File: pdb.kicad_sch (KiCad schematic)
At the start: 0 parts

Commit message: first commit branch
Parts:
- added F1: Fuse, Library:FUSE-TH_XF-508P-A-B, symbol Device:Fuse
- added J1: Amass Elec AS150UPW(2+4), Library:CONN-TH_AS150UPW, symbol Connector:Conn_01x06_Pin
- added J2, J3, J4, J5: BOOMELE 4.2-2*3AW, Connector_Molex:Molex_Mini-Fit_Jr_5569-06A2_2x03_P4.20mm_Horizontal, symbol Connector:Conn_01x06_Pin
- added J6: Conn_01x08_Pin, symbol Connector:Conn_01x08_Pin
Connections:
- new net +BATT: F1.1, J1.2 (Pin_2)
- new net CAN_H_1: J1.3 (Pin_3), J2.1 (Pin_1)
- new net CAN_H_2: J2.3 (Pin_3), J3.1 (Pin_1)
- new net CAN_H_3: J3.3 (Pin_3), J4.1 (Pin_1)
- new net CAN_H_4: J4.3 (Pin_3), J5.1 (Pin_1)
- new net CAN_H_5: J5.3 (Pin_3), J6.3 (Pin_3)
- new net CAN_H_6: J6.5 (Pin_5)
- new net CAN_L_1: J1.4 (Pin_4), J2.2 (Pin_2)
- new net CAN_L_2: J2.4 (Pin_4), J3.2 (Pin_2)
- new net CAN_L_3: J3.4 (Pin_4), J4.2 (Pin_2)
- new net CAN_L_4: J4.4 (Pin_4), J5.2 (Pin_2)
- new net CAN_L_5: J5.4 (Pin_4), J6.4 (Pin_4)
- new net CAN_L_6: J6.6 (Pin_6)
- new net GND: J1.1 (Pin_1), J2.6 (Pin_6), J3.6 (Pin_6), J4.6 (Pin_6), J5.6 (Pin_6), J6.1 (Pin_1), J6.7 (Pin_7)
- new net PWM_Mot_BL: J5.5 (Pin_5)
- new net PWM_Mot_BR: J4.5 (Pin_5)
- new net PWM_Mot_FL: J3.5 (Pin_5)
- new net PWM_Mot_FR: J2.5 (Pin_5)
- new net PWM_Pump: J6.2 (Pin_2)
- new net VBat: F1.2
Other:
- note added: "Comienza el CAN BUS"
- note added: "MotorBL"
- note added: "MotorBR"
- note added: "MotorFL"
- note added: "MotorFR"
- note added: "Pump"

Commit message: ADD: Mas conectores al esquematico y fuse holder para 10x38
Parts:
- added J10, J16, J7, J8, J9: BOOMELE 4.2-2*4AW, symbol Connector:Conn_01x08_Pin
- added J11: MOLEX 39301240, symbol Connector:Conn_01x24_Pin
- added J12, J13: BOOMELE 4.2-2*2AW, symbol Connector:Conn_01x04_Pin
- added J14, J15: BOOMELE 4.2-2*3AW, Connector_Molex:Molex_Mini-Fit_Jr_5569-06A2_2x03_P4.20mm_Horizontal, symbol Connector:Conn_01x06_Pin
- F1: footprint Library:FUSE-TH_XF-508P-A-B -> Library:FUSE-HOLDER XFCN XF-008; LCSC Part # C19727304 -> C717029
- J6: value Conn_01x08_Pin -> BOOMELE 4.2-2*4AW; LCSC Part # (none) -> C44253
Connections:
- net CAN_H_6: now also J7.3 (Pin_3)
- net CAN_L_6: now also J7.4 (Pin_4)
- net GND: now also J10.1 (Pin_1), J10.7 (Pin_7), J12.2 (Pin_2), J12.4 (Pin_4), J13.2 (Pin_2), J13.4 (Pin_4), J14.2 (Pin_2), J14.5 (Pin_5), J15.2 (Pin_2), J15.5 (Pin_5), J16.1 (Pin_1), J16.8 (Pin_8), J7.1 (Pin_1), J7.7 (Pin_7), J8.1 (Pin_1), J8.7 (Pin_7), J9.1 (Pin_1), J9.7 (Pin_7)
- net VBat: now also J6.8 (Pin_8), J10.8 (Pin_8), J12.1 (Pin_1), J13.1 (Pin_1), J7.8 (Pin_8), J8.8 (Pin_8), J9.8 (Pin_8)
- new net +24V: J16.2 (Pin_2)
- new net +5V: J14.1 (Pin_1), J15.1 (Pin_1)
- new net CAMERA_RX: J16.3 (Pin_3)
- new net CAMERA_Sbus_in: J16.6 (Pin_6)
- new net CAMERA_Sbus_out: J16.5 (Pin_5)
- new net CAMERA_TX: J16.4 (Pin_4)
- new net CAN_H_10: J10.5 (Pin_5)
- new net CAN_H_7: J7.5 (Pin_5), J8.3 (Pin_3)
- new net CAN_H_8: J8.5 (Pin_5), J9.3 (Pin_3)
- new net CAN_H_9: J10.3 (Pin_3), J9.5 (Pin_5)
- new net CAN_L_10: J10.6 (Pin_6)
- new net CAN_L_7: J7.6 (Pin_6), J8.4 (Pin_4)
- new net CAN_L_8: J8.6 (Pin_6), J9.4 (Pin_4)
- new net CAN_L_9: J10.4 (Pin_4), J9.6 (Pin_6)
- new net LIDAR_1_RX_SCL: J14.3 (Pin_3)
- new net LIDAR_1_TX_SDA: J14.4 (Pin_4)
- new net LIDAR_2_RX_SCL: J15.3 (Pin_3)
- new net LIDAR_2_TX_SDA: J15.4 (Pin_4)
- new net PWM_Asp_BL: J10.2 (Pin_2)
- new net PWM_Asp_BR: J9.2 (Pin_2)
- new net PWM_Asp_FL: J8.2 (Pin_2)
- new net PWM_Asp_FR: J7.2 (Pin_2)
- new net PWM_Light: J12.3 (Pin_3), J13.3 (Pin_3)
- no-connect marks 0 -> 2
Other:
- note added: "AspBL"
- note added: "AspBR"
- note added: "AspFL"
- note added: "AspFR"
- note added: "BOM x2"
- note added: "Camera"
- note added: "Lidar 1"
- note added: "Lidar 2"
- note added: "Light 1"
- note added: "Light 2"
- note added: "Veronte"
- moved on the sheet: J6

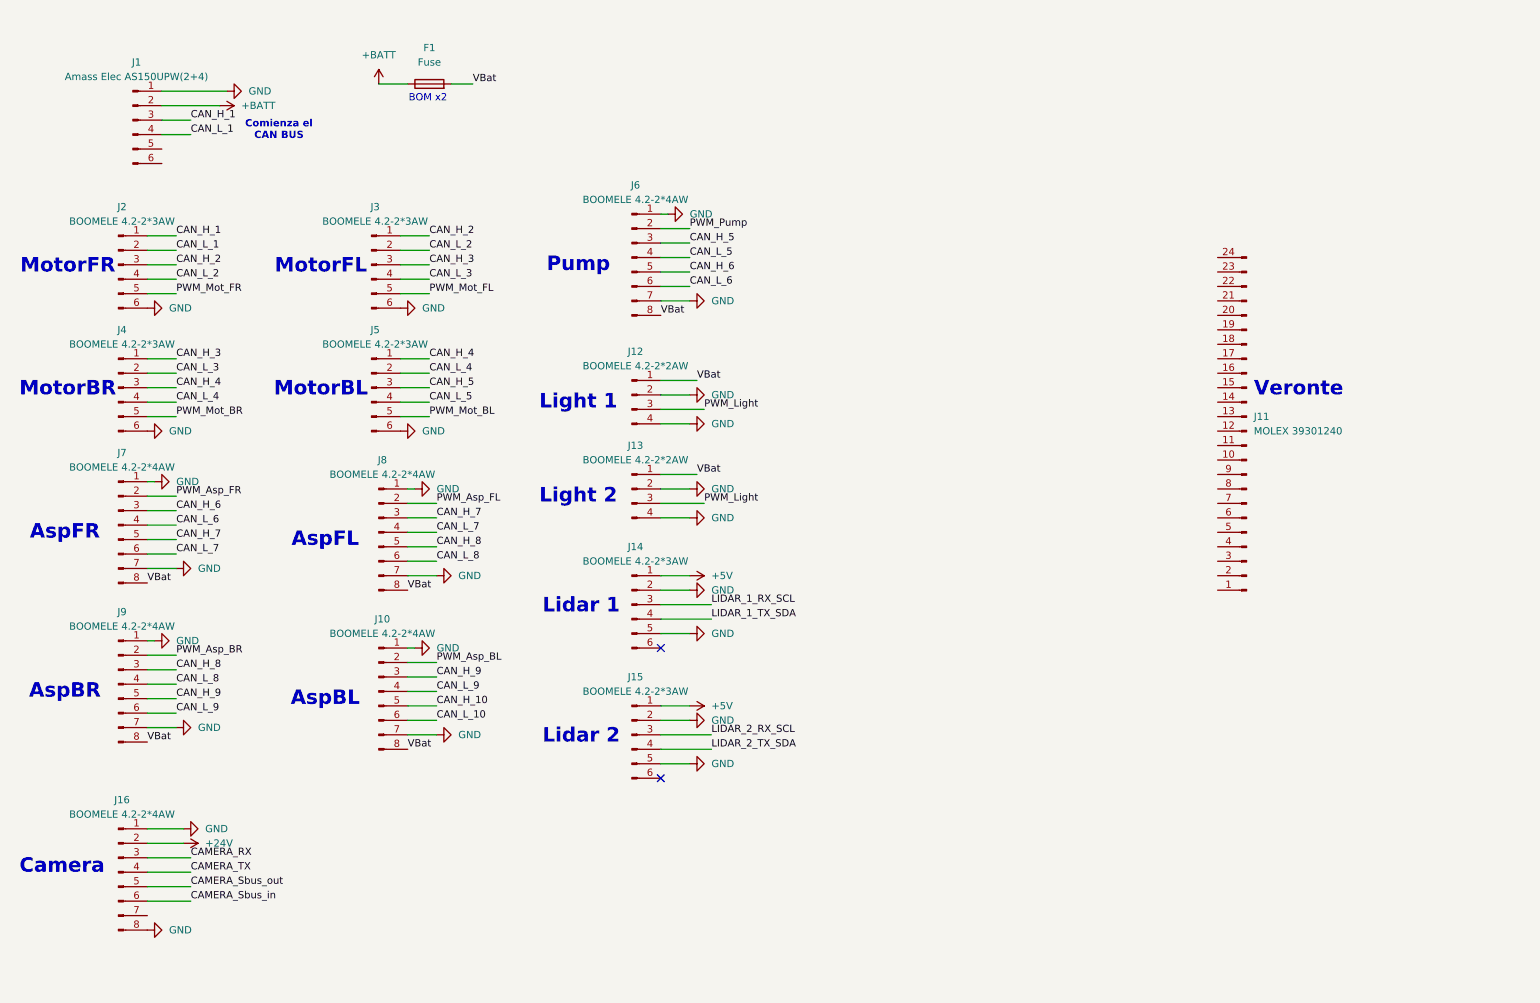
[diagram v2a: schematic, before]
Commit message: Esquematico casi terminado falta agregar el veronte
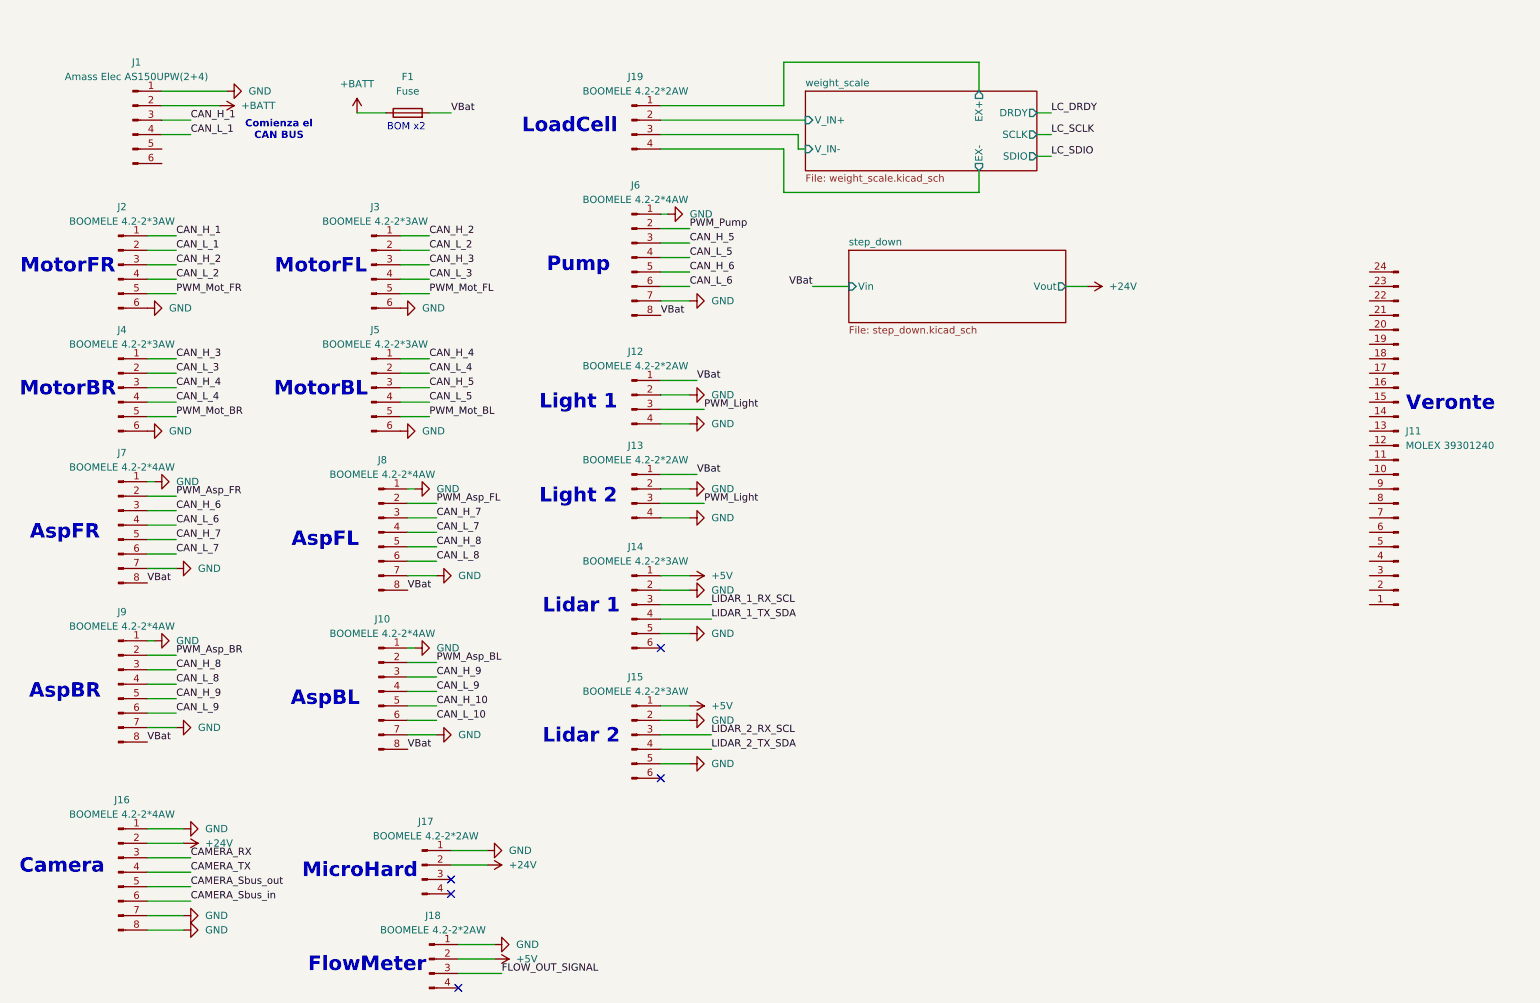
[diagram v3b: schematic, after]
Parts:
- added J17, J18, J19: BOOMELE 4.2-2*2AW, Connector_Molex:Molex_Mini-Fit_Jr_5569-04A2_2x02_P4.20mm_Horizontal, symbol Connector:Conn_01x04_Pin
- J10, J16, J6, J7, J8, J9: footprint (none) -> Connector_Molex:Molex_Mini-Fit_Jr_5569-08A2_2x04_P4.20mm_Horizontal
- J11: footprint (none) -> Connector_Molex:Molex_Mini-Fit_Jr_5569-24A2_2x12_P4.20mm_Horizontal
- J12, J13: footprint (none) -> Connector_Molex:Molex_Mini-Fit_Jr_5569-04A2_2x02_P4.20mm_Horizontal
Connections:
- net +24V: now also J17.2 (Pin_2)
- net +5V: now also J18.2 (Pin_2)
- net GND: now also J16.7 (Pin_7), J17.1 (Pin_1), J18.1 (Pin_1)
- new net FLOW_OUT_SIGNAL: J18.3 (Pin_3)
- new net weight_scale/EX+: J19.1 (Pin_1)
- new net weight_scale/EX-: J19.4 (Pin_4)
- new net weight_scale/V_IN+: J19.2 (Pin_2)
- new net weight_scale/V_IN-: J19.3 (Pin_3)
- no-connect marks 2 -> 5
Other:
- added sheet step_down (step_down.kicad_sch)
- added sheet weight_scale (weight_scale.kicad_sch)
- note added: "FlowMeter"
- note added: "LoadCell"
- note added: "MicroHard"
- moved on the sheet: F1, J11

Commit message: ADD: Fuente de 24V a 5V para los Lidar
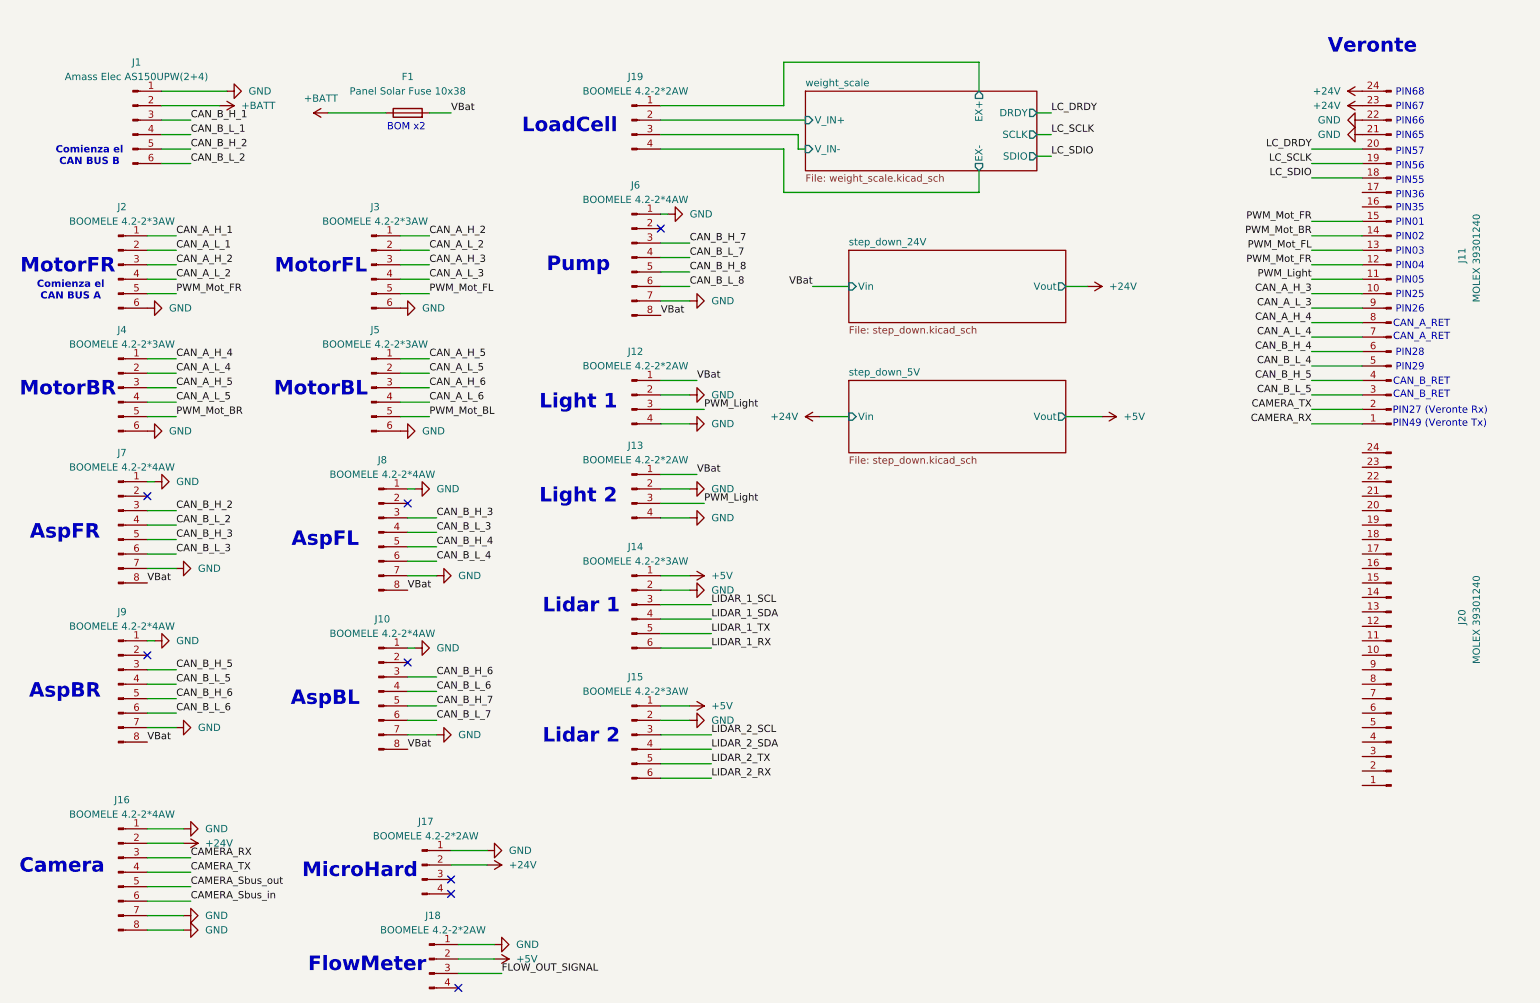
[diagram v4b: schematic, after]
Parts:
- added J20: MOLEX 39301240, Connector_Molex:Molex_Mini-Fit_Jr_5569-24A2_2x12_P4.20mm_Horizontal, symbol Connector:Conn_01x24_Pin
- F1: value Fuse -> Panel Solar Fuse 10x38
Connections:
- net +24V: now also J11.23 (Pin_23), J11.24 (Pin_24)
- net CAMERA_RX: now also J11.1 (Pin_1)
- net CAMERA_TX: now also J11.2 (Pin_2)
- net GND: now also J11.21 (Pin_21), J11.22 (Pin_22); no longer J14.5 (Pin_5), J15.5 (Pin_5)
- net LC_DRDY: now also J11.20 (Pin_20)
- net LC_SCLK: now also J11.19 (Pin_19)
- net LC_SDIO: now also J11.18 (Pin_18)
- net PWM_Light: now also J11.11 (Pin_11)
- net PWM_Mot_BR: now also J11.14 (Pin_14)
- net PWM_Mot_FL: now also J11.13 (Pin_13)
- net PWM_Mot_FR: now also J11.12 (Pin_12), J11.15 (Pin_15)
- net LIDAR_1_RX: now reaches J14.6 (Pin_6)
- net CAN_A_H_3: now reaches J11.10 (Pin_10)
- net CAN_A_H_3: now also J3.3 (Pin_3)
- net CAN_B_L_5: now reaches J11.3 (Pin_3)
- net CAN_B_L_5: now also J9.4 (Pin_4)
- net CAN_B_H_5: now reaches J11.4 (Pin_4)
- net CAN_B_H_5: now also J9.3 (Pin_3)
- net CAN_B_L_4: now reaches J11.5 (Pin_5)
- net CAN_B_L_4: now also J8.6 (Pin_6)
- net CAN_B_H_4: now reaches J11.6 (Pin_6)
- net CAN_B_H_4: now also J8.5 (Pin_5)
- net CAN_A_L_4: now reaches J11.7 (Pin_7)
- net CAN_A_L_4: now also J4.2 (Pin_2)
- net CAN_A_H_4: now reaches J11.8 (Pin_8)
- net CAN_A_H_4: now also J4.1 (Pin_1)
- net CAN_A_L_3: now reaches J11.9 (Pin_9)
- net CAN_A_L_3: now also J3.4 (Pin_4)
- net CAN_B_H_2: now reaches J1.5 (Pin_5)
- net CAN_B_H_2: now also J7.3 (Pin_3)
- net CAN_B_L_2: now reaches J1.6 (Pin_6)
- net CAN_B_L_2: now also J7.4 (Pin_4)
- net LIDAR_2_RX: now reaches J15.6 (Pin_6)
- net CAN_H_1 renamed CAN_A_H_1
- net CAN_A_H_1: no longer J1.3 (Pin_3)
- net CAN_H_10 renamed CAN_B_H_7
- net CAN_B_H_7: now also J6.3 (Pin_3)
- net CAN_H_2 renamed CAN_A_H_2
- removed net CAN_H_3: J3.3 (Pin_3), J4.1 (Pin_1)
- net CAN_H_4 renamed CAN_A_H_5
- net CAN_H_5 renamed CAN_A_H_6
- net CAN_A_H_6: no longer J6.3 (Pin_3)
- net CAN_H_6 renamed CAN_B_H_8
- net CAN_B_H_8: no longer J7.3 (Pin_3)
- net CAN_H_7 renamed CAN_B_H_3
- removed net CAN_H_8: J8.5 (Pin_5), J9.3 (Pin_3)
- net CAN_H_9 renamed CAN_B_H_6
- net CAN_L_1 renamed CAN_A_L_1
- net CAN_A_L_1: no longer J1.4 (Pin_4)
- net CAN_L_10 renamed CAN_B_L_7
- net CAN_B_L_7: now also J6.4 (Pin_4)
- net CAN_L_2 renamed CAN_A_L_2
- removed net CAN_L_3: J3.4 (Pin_4), J4.2 (Pin_2)
- net CAN_L_4 renamed CAN_A_L_5
- net CAN_L_5 renamed CAN_A_L_6
- net CAN_A_L_6: no longer J6.4 (Pin_4)
- net CAN_L_6 renamed CAN_B_L_8
- net CAN_B_L_8: no longer J7.4 (Pin_4)
- net CAN_L_7 renamed CAN_B_L_3
- removed net CAN_L_8: J8.6 (Pin_6), J9.4 (Pin_4)
- net CAN_L_9 renamed CAN_B_L_6
- net LIDAR_1_RX_SCL renamed LIDAR_1_SCL
- net LIDAR_1_TX_SDA renamed LIDAR_1_SDA
- net LIDAR_2_RX_SCL renamed LIDAR_2_SCL
- net LIDAR_2_TX_SDA renamed LIDAR_2_SDA
- net PWM_Asp_BL: no longer names the net of J10.2 (Pin_2)
- net PWM_Asp_BR: no longer names the net of J9.2 (Pin_2)
- net PWM_Asp_FL: no longer names the net of J8.2 (Pin_2)
- net PWM_Asp_FR: no longer names the net of J7.2 (Pin_2)
- net PWM_Pump: no longer names the net of J6.2 (Pin_2)
- new net CAN_B_H_1: J1.3 (Pin_3)
- new net CAN_B_L_1: J1.4 (Pin_4)
- new net LIDAR_1_TX: J14.5 (Pin_5)
- new net LIDAR_2_TX: J15.5 (Pin_5)
- no-connect marks 5 -> 8
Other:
- sheet step_down renamed step_down_24V
- added sheet step_down_5V (step_down.kicad_sch)
- note added: "CAN_A_RET"
- note added: "CAN_B_RET"
- note added: "Comienza el CAN BUS A"
- note added: "Comienza el CAN BUS B"
- note added: "PIN01"
- note added: "PIN02"
- note added: "PIN03"
- note added: "PIN04"
- note added: "PIN05"
- note added: "PIN25"
- note added: "PIN26"
- note added: "PIN27 (Veronte Rx)"
- note added: "PIN28"
- note added: "PIN29"
- note added: "PIN35"
- note added: "PIN36"
- note added: "PIN49 (Veronte Tx)"
- note added: "PIN55"
- note added: "PIN56"
- note added: "PIN57"
- note added: "PIN65"
- note added: "PIN66"
- note added: "PIN67"
- note added: "PIN68"
- note removed: "Comienza el CAN BUS"
- moved on the sheet: J11
